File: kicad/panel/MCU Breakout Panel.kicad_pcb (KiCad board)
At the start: 2 copper layers, 67 x 77.5 mm, 10 parts

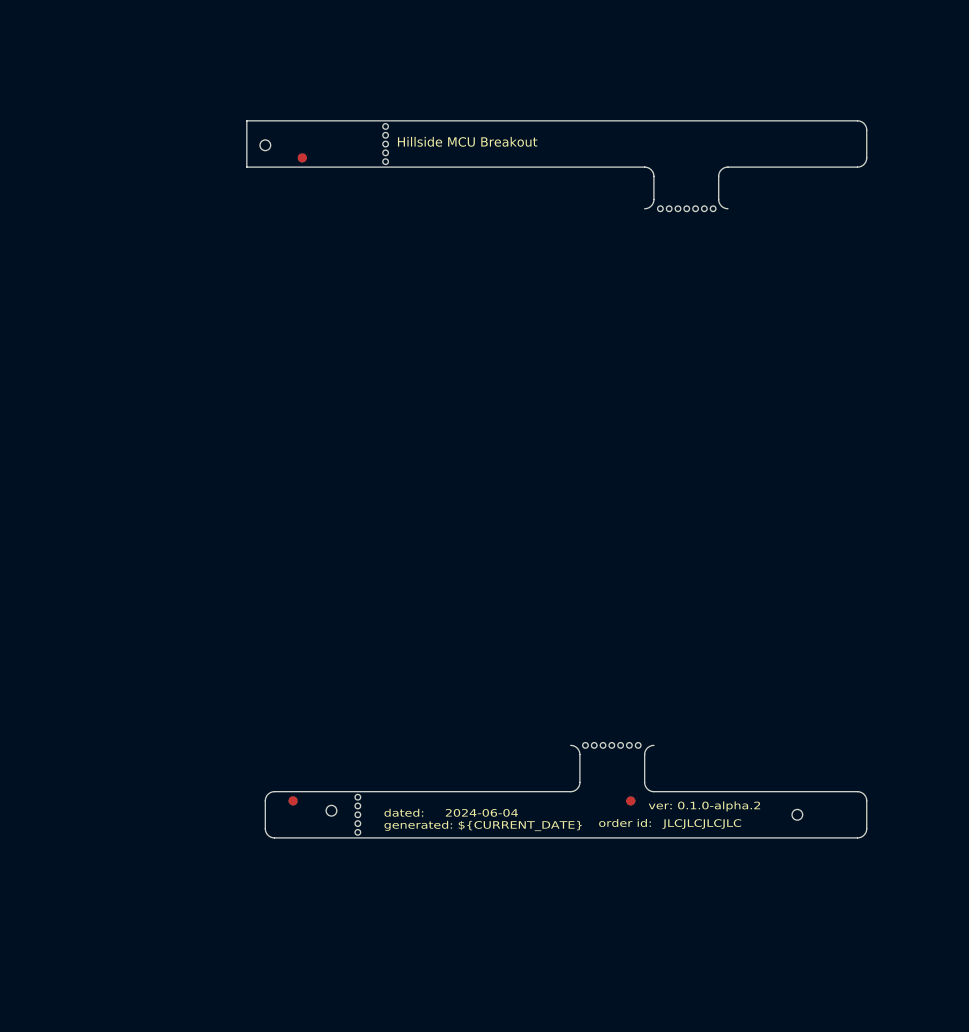
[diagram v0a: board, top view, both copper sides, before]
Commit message: feat(panel): import left and right sides
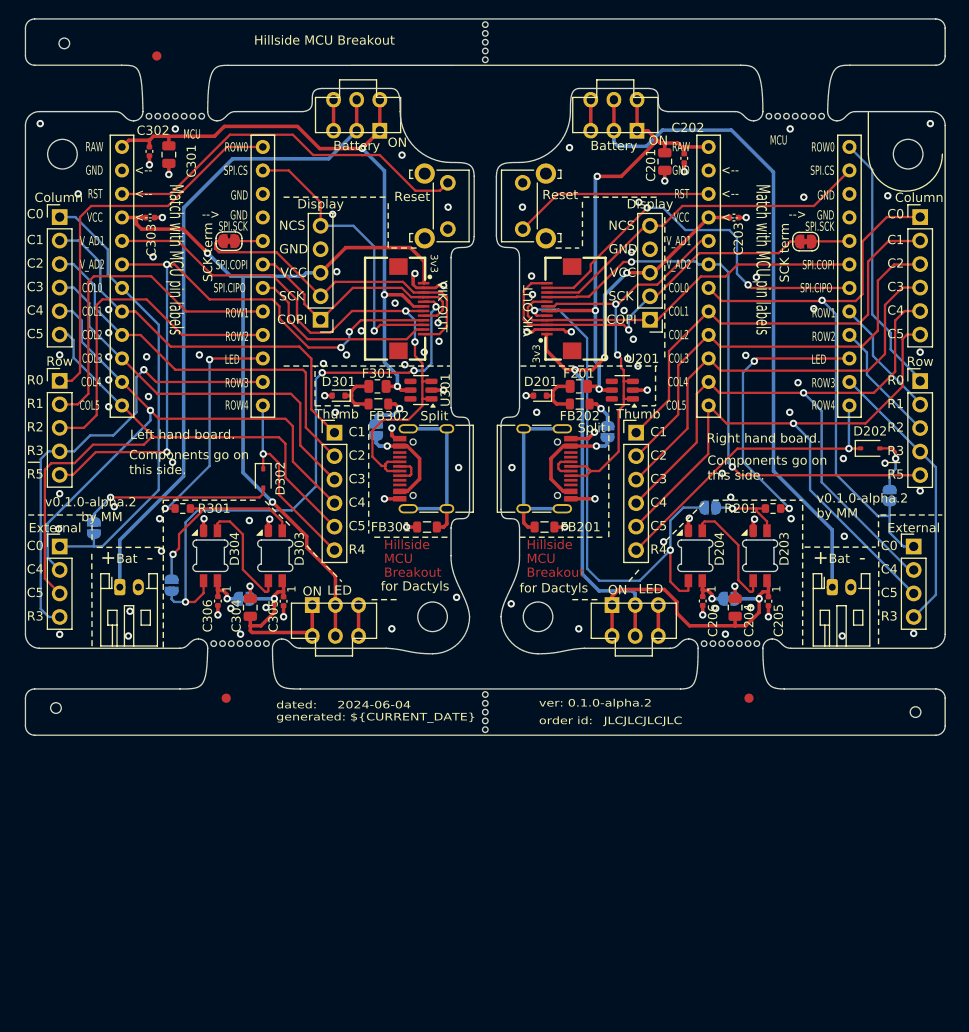
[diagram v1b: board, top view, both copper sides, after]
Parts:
- removed the REF** at (158.5, 127.5)
- removed the REF** at (166.6, 69.5)
- added C201: 4.7uF, Capacitor_SMD:C_0805_2012Metric, F.Cu at (164.2, 64.4)
- added C202: 0.1uF, Capacitor_SMD:C_0402_1005Metric, F.Cu at (166.3, 64.0)
- added C203: 0.1uF, Capacitor_SMD:C_0402_1005Metric, F.Cu at (171.7, 70.5)
- added C204: 22uF, Capacitor_SMD:C_0805_2012Metric, F.Cu at (171.8, 112.6)
- added C205: 0.1uF, Capacitor_SMD:C_0402_1005Metric, F.Cu at (175.4, 111.9)
- added C206: 0.1uF, Capacitor_SMD:C_0402_1005Metric, F.Cu at (168.3, 111.9)
- added C301: 4.7uF, Capacitor_SMD:C_0805_2012Metric, F.Cu at (110.6, 63.6)
- added C302: 0.1uF, Capacitor_SMD:C_0402_1005Metric, F.Cu at (108.5, 63.3)
- added C303: 0.1uF, Capacitor_SMD:C_0402_1005Metric, F.Cu at (108.6, 70.5)
- added C304: 22uF, Capacitor_SMD:C_0805_2012Metric, F.Cu at (119.4, 112.6)
- added C305: 0.1uF, Capacitor_SMD:C_0402_1005Metric, F.Cu at (123.0, 111.9)
- added C306: 0.1uF, Capacitor_SMD:C_0402_1005Metric, F.Cu at (115.9, 111.9)
- added D201: ESD5Z5V0, Diode_SMD:D_SOD-523, F.Cu at (150.7, 89.7)
- added D202: D_Small, Diode_SMD:D_SOD-323, F.Cu at (186.4, 95.4)
- added D203: SK6812-MINI-E, Dactyl:SK6812-MINI-E-Dog2_1S, F.Cu at (174.5, 107.0)
- added D204: SK6812-MINI-E, Dactyl:SK6812-MINI-E-Dog2_1S, F.Cu at (167.5, 107.0)
- added D301: ESD5Z5V0, Diode_SMD:D_SOD-523, F.Cu at (128.9, 89.7)
- added D302: D_Small, Diode_SMD:D_SOD-323, F.Cu at (120.8, 98.7)
- added D303: SK6812-MINI-E, Dactyl:SK6812-MINI-E-Dog2_1S, F.Cu at (122.1, 107.0)
- added D304: SK6812-MINI-E, Dactyl:SK6812-MINI-E-Dog2_1S, F.Cu at (115.1, 107.0)
- added F201: 750mA 6V Polyfuse, Fuse:Fuse_0805_2012Metric, F.Cu at (154.9, 88.7)
- added F301: 750mA 6V Polyfuse, Fuse:Fuse_0805_2012Metric, F.Cu at (133.1, 88.7)
- added FB201: 20mΩ 100Ω@100MHz, Inductor_SMD:L_0805_2012Metric, F.Cu at (151.2, 103.9)
- added FB202: 20mΩ 100Ω@100MHz, Inductor_SMD:L_0805_2012Metric, F.Cu at (155.0, 90.6)
- added FB301: 20mΩ 100Ω@100MHz, Inductor_SMD:L_0805_2012Metric, F.Cu at (138.5, 103.9)
- added FB302: 20mΩ 100Ω@100MHz, Inductor_SMD:L_0805_2012Metric, F.Cu at (133.2, 90.6)
- added H201: MountingHole, Dactyl_basics:MountingHole_3.2mm_M3_DIN965, F.Cu at (190.5, 63.6)
- added H202: MountingHole, Dactyl_basics:MountingHole_3.2mm_M3_DIN965, F.Cu at (150.5, 113.6)
- added H301: MountingHole, Dactyl_basics:MountingHole_3.2mm_M3_DIN965, F.Cu at (99.1, 63.6)
- added H302: MountingHole, Dactyl_basics:MountingHole_3.2mm_M3_DIN965, F.Cu at (139.1, 113.6)
- added J201: JST, Dactyl:JST_PH_S2B-PH-K_1x02_P2.00mm_Horizontal, F.Cu at (182.3, 110.4)
- added J202: Split, Dactyl_basics:USB_C_Receptacle_HRO_TYPE-C-31-M-12, F.Cu at (150.0, 97.6)
- added J203: Column, Dactyl:PinHeader_Columns, F.Cu at (191.8, 70.4)
- added J204: Thumb, Dactyl:PinHeader_Thumbs, F.Cu at (161.1, 93.7)
- added J205: External, Dactyl:PinHeader_External, F.Cu at (191.1, 106.0)
- added J206: Row, Dactyl:PinHeader_Rows, F.Cu at (191.8, 88.1)
- added J207: Display, Dactyl:PinHeader_Display, F.Cu at (162.6, 81.5)
- added J208: Vic, Dactyl:vik-keyboard-connector-horizontal, F.Cu at (153.5, 80.3)
- added J301: JST, Dactyl:JST_PH_S2B-PH-K_1x02_P2.00mm_Horizontal, F.Cu at (105.3, 110.4)
- added J302: Split, Dactyl_basics:USB_C_Receptacle_HRO_TYPE-C-31-M-12, F.Cu at (139.6, 97.6)
- added J303: Column, Dactyl:PinHeader_Columns, F.Cu at (98.8, 70.4)
- added J304: Thumb, Dactyl:PinHeader_Thumbs, F.Cu at (128.5, 93.7)
- added J305: External, Dactyl:PinHeader_External, F.Cu at (98.8, 106.0)
- added J306: Row, Dactyl:PinHeader_Rows, F.Cu at (98.8, 88.1)
- added J307: Display, Dactyl:PinHeader_Display, F.Cu at (127.0, 81.5)
- added J308: Vic, Dactyl:vik-keyboard-connector-horizontal, F.Cu at (136.1, 80.3)
- added JP201: Split power, Dactyl_basics:SolderJumper-2_P1.3mm_Open_RoundedPad1.0x1.5mm, B.Cu at (158.0, 93.6)
- added JP202: Wired Left, Dactyl_basics:SolderJumper-2_P1.3mm_Open_RoundedPad1.0x1.5mm, B.Cu at (188.5, 100.5)
- added JP203: SCK term, Dactyl_basics:SolderJumper-2_P1.3mm_Bridged_RoundedPad1.0x1.5mm, F.Cu at (179.4, 73.0)
- added JP204: Vik LED bypass, Dactyl_basics:SolderJumper-2_P1.3mm_Open_RoundedPad1.0x1.5mm, B.Cu at (169.1, 101.8)
- added JP205: LED2 power, Dactyl_basics:SolderJumper-2_P1.3mm_Bridged_RoundedPad1.0x1.5mm, B.Cu at (171.2, 111.7)
- added JP301: Split power, Dactyl_basics:SolderJumper-2_P1.3mm_Open_RoundedPad1.0x1.5mm, B.Cu at (133.0, 93.4)
- added JP302: Wired Left, Dactyl_basics:SolderJumper-2_P1.3mm_Open_RoundedPad1.0x1.5mm, B.Cu at (102.5, 104.0)
- added JP303: SCK term, Dactyl_basics:SolderJumper-2_P1.3mm_Bridged_RoundedPad1.0x1.5mm, F.Cu at (117.1, 73.0)
- added JP304: Vik LED bypass, Dactyl_basics:SolderJumper-2_P1.3mm_Open_RoundedPad1.0x1.5mm, B.Cu at (110.9, 110.2)
- added JP305: LED2 power, Dactyl_basics:SolderJumper-2_P1.3mm_Bridged_RoundedPad1.0x1.5mm, B.Cu at (118.8, 111.7)
- added R201: 300 Ohm, Resistor_SMD:R_0603_1608Metric, F.Cu at (175.9, 101.9)
- added R301: 300 Ohm, Resistor_SMD:R_0603_1608Metric, F.Cu at (112.1, 101.9)
- added REF**: Mouse_Bites, Dactyl_basics:Mouse_Bites, F.Cu at (171.3, 116.5)
- added REF**: Mouse_Bites, Dactyl_basics:Mouse_Bites, F.Cu at (118.3, 116.5)
- added REF**: Mouse_Bites, Dactyl_basics:Mouse_Bites, F.Cu at (178.3, 59.5)
- added REF**: Mouse_Bites, Dactyl_basics:Mouse_Bites, F.Cu at (111.3, 59.5)
- added REF**: art_name, Dactyl:art_name, F.Cu at (152.5, 107.4)
- added REF**: art_name, Dactyl:art_name, F.Cu at (137.1, 107.4)
- added SW201: Battery, Dactyl:SW_SPDT_Battery, F.Cu at (158.7, 59.4)
- added SW202: Reset, Dactyl_basics:SW_Tactile_SKHL_Angled, F.Cu at (150.1, 69.2)
- added SW203: LED, Dactyl:SW_SPDT_JS202011AQN_wider, F.Cu at (161.0, 114.0)
- added SW301: Battery, Dactyl:SW_SPDT_Battery, F.Cu at (130.9, 59.4)
- added SW302: Reset, Dactyl_basics:SW_Tactile_SKHL_Angled, F.Cu at (139.5, 69.2)
- added SW303: LED, Dactyl:SW_SPDT_JS202011AQN_wider, F.Cu at (128.6, 114.0)
- added U201: SRV05-4, Package_TO_SOT_SMD:SOT-23-6, F.Cu at (159.6, 89.1)
- added U202: Nice!Nano/2040, Dactyl:ProMicro_v2_1S, F.Cu at (176.5, 77.3)
- added U301: SRV05-4, Package_TO_SOT_SMD:SOT-23-6, F.Cu at (137.8, 89.1)
- added U302: Nice!Nano/2040, Dactyl:ProMicro_v2_1S, F.Cu at (113.1, 77.3)
- moved H4 31.8 mm to (98.4, 123.5)
- moved H3 24.4 mm to (99.3, 51.6)
- moved FID1 19.2 mm to (109.3, 53.0)
- moved REF** 17.7 mm to (144.8, 123.9)
- moved FID3 16.9 mm to (173.3, 122.4)
- moved H5 16.9 mm to (191.3, 123.9)
- moved REF** 15.4 mm to (144.8, 51.5)
- moved FID2 13.2 mm to (116.8, 122.4)
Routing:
- net /Left/VCC: track 0.00 -> 80.7 mm, vias 0 -> 2
- net /Left/row5_VIK_GP_AD2: track 0.00 -> 71.7 mm, vias 0 -> 4
- net /Right/col4: track 0.00 -> 70.9 mm, vias 0 -> 1
- net /Right/col5: track 0.00 -> 70.8 mm, vias 0 -> 1
- net /Left/col5: track 0.00 -> 68.8 mm
- net /Right/bat+: track 0.00 -> 68.8 mm
- net /Left/RAW: track 0.00 -> 67.2 mm, vias 0 -> 3
- net /Left/SPLIT_VIK_GP_AD1: track 0.00 -> 66.8 mm, vias 0 -> 2
- net /Left/bat+: track 0.00 -> 66.0 mm
- net /Left/col4: track 0.00 -> 64.3 mm, vias 0 -> 1
- net /Right/col0: track 0.00 -> 64.2 mm, vias 0 -> 1
- net /Right/VCC: track 0.00 -> 64.0 mm, vias 0 -> 3
- net /Right/row5_VIK_GP_AD2: track 0.00 -> 63.6 mm, vias 0 -> 2
- net /Left/LED_out: track 0.00 -> 63.5 mm, vias 0 -> 4
- net /Right/LED_out: track 0.00 -> 59.0 mm, vias 0 -> 2
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- added copper zone on In1.Cu, net /Left/GND
- added copper zone on In2.Cu, net /Left/GND
- added copper zone on In1.Cu, net /Right/GND
- added copper zone on In2.Cu, net /Right/GND
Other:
- board size 67 x 77.5 mm -> 99.4 x 77.4 mm
- copper layers 2 -> 4
- board text added: "Components go on other side."
- board text added: "Components go on this side."
- board text added: "Hillside MCU Breakout"
- board text added: "Left hand board."
- board text added: "Right hand board."
- board text added: "for Dactyls"
- board text added: "v${REVISION}"
- board text added: "v${REVISION} by MM"

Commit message: feat(panel): import left and right boards
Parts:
- moved JP204 30.0 mm to (169.1, 131.8)
- moved C301 30.0 mm to (110.6, 93.7)
- moved FID1 30.0 mm to (109.3, 83.0)
- moved SW201 30.0 mm to (158.7, 89.4)
- moved SW301 30.0 mm to (130.9, 89.4)
- moved C201 30.0 mm to (164.2, 94.4)
- moved C202 30.0 mm to (166.3, 94.0)
- moved C203 30.0 mm to (171.7, 100.5)
- moved C204 30.0 mm to (171.8, 142.6)
- moved C206 30.0 mm to (168.3, 141.9)
- moved C302 30.0 mm to (108.5, 93.3)
- moved C303 30.0 mm to (108.6, 100.5)
- moved C304 30.0 mm to (119.4, 142.6)
- moved C306 30.0 mm to (115.9, 141.9)
- moved D201 30.0 mm to (150.7, 119.7)
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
